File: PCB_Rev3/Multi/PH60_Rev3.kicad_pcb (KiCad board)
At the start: 2 copper layers, 285 x 94.6 mm, 164 parts, among them J1 USB_C_Receptacle_USB2.0_16P

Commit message: muliti layout
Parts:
- removed the S41-x1 at (292.9, 76.2)
- added AE1: Antenna, Library:nrf52_ant_1.6mm, B.Cu at (35.5, 67.4)
- added BT1: Battery, Connector_Molex:Molex_PicoBlade_53261-0271_1x02-1MP_P1.25mm_Horizontal, B.Cu at (231.1, 56.0)
- added C1: 100n, Capacitor_SMD:C_0402_1005Metric, B.Cu at (49.4, 61.9)
- added C10: 12p, Capacitor_SMD:C_0402_1005Metric, B.Cu at (54.2, 60.0)
- added C11: 20u, Capacitor_SMD:C_0402_1005Metric, B.Cu at (12.6, 22.8)
- added C12: 0.5p, Capacitor_SMD:C_0402_1005Metric, B.Cu at (38.5, 65.7)
- added C13: 0.8p, Capacitor_SMD:C_0402_1005Metric, B.Cu at (41.8, 67.0)
- added C14: 12p, Capacitor_SMD:C_0402_1005Metric, B.Cu at (51.1, 74.0)
- added C15: 12p, Capacitor_SMD:C_0402_1005Metric, B.Cu at (49.0, 72.1)
- added C16: 1u, Capacitor_SMD:C_0402_1005Metric, B.Cu at (110.6, 143.8)
- added C17: 47n, Capacitor_SMD:C_0603_1608Metric, B.Cu at (94.2, 138.1)
- added C18: 4u7, Capacitor_SMD:C_0402_1005Metric, B.Cu at (110.6, 145.7)
- added C19: 1u, Capacitor_SMD:C_0402_1005Metric, B.Cu at (110.6, 147.7)
- added C2: 820p, Capacitor_SMD:C_0402_1005Metric, B.Cu at (54.3, 71.7)
- added C20: 100n, Capacitor_SMD:C_0402_1005Metric, B.Cu at (107.7, 137.9)
- added C21: 100n, Capacitor_SMD:C_0402_1005Metric, B.Cu at (107.7, 139.8)
- added C22: 100n, Capacitor_SMD:C_0402_1005Metric, B.Cu at (107.7, 141.8)
- added C3: 4u7, Capacitor_SMD:C_0402_1005Metric, B.Cu at (60.6, 60.4)
- added C4: 100p, Capacitor_SMD:C_0402_1005Metric, B.Cu at (53.2, 71.7)
- added C5: 4u7, Capacitor_SMD:C_0402_1005Metric, B.Cu at (60.4, 64.3)
- added C6: 4u7, Capacitor_SMD:C_0402_1005Metric, B.Cu at (60.6, 59.4)
- added C7: 4u7, Capacitor_SMD:C_0402_1005Metric, B.Cu at (56.6, 60.4)
- added C8: 12p, Capacitor_SMD:C_0402_1005Metric, B.Cu at (48.9, 59.9)
- added C9: 10u, Capacitor_SMD:C_0402_1005Metric, B.Cu at (12.6, 20.9)
- added D14-1: DIODE, Diode_SMD:D_SOD-123, B.Cu at (277.2, 46.4)
- added D61: DIODE, Diode_SMD:D_SOD-123, B.Cu at (120.8, 106.7)
- added D63: DIODE, Diode_SMD:D_SOD-123, B.Cu at (180.7, 107.5)
- added D68: PTVS5V0P1UP, PCM_Diode_SMD_AKL:D_SOD-882_DFN1006-2, B.Cu at (9.80, 21.2)
- added J1: Conn_01x02_Pin, Connector_PinHeader_2.00mm:PinHeader_1x02_P2.00mm_Vertical, B.Cu at (30.4, 81.0)
- added J2: Conn_01x02_Pin, Connector_PinHeader_2.00mm:PinHeader_1x02_P2.00mm_Vertical, B.Cu at (30.4, 73.7)
- added J4: Conn_01x04_Socket, Connector_FFC-FPC:Molex_200528-0040_1x04-1MP_P1.00mm_Horizontal, B.Cu at (97.0, 23.4)
- added L1: MCL1608S100MT, Inductor_SMD:L_0603_1608Metric, B.Cu at (57.9, 59.8)
- added L2: 2.2uH, Inductor_SMD:L_Changjiang_FNR252012S, B.Cu at (15.0, 18.1)
- added L3: FHW0402UC4N7JST, Inductor_SMD:L_0402_1005Metric, B.Cu at (40.1, 67.4)
- added L4: LQG15HS15NJ02D, Inductor_SMD:L_0402_1005Metric, B.Cu at (93.4, 149.9)
- added L5: MCL1608S100MT, Inductor_SMD:L_0603_1608Metric, B.Cu at (94.2, 143.1)
- added R10: 10k, PCM_Resistor_SMD_AKL:R_0402_1005Metric, B.Cu at (24.9, 41.4)
- added R12: 10k, PCM_Resistor_SMD_AKL:R_0402_1005Metric, B.Cu at (15.5, 20.9)
- added R13: 10k, PCM_Resistor_SMD_AKL:R_0402_1005Metric, B.Cu at (15.5, 23.1)
- added R14: 10k, PCM_Resistor_SMD_AKL:R_0402_1005Metric, B.Cu at (21.5, 17.6)
- added R15: 10k, PCM_Resistor_SMD_AKL:R_0402_1005Metric, B.Cu at (21.5, 19.7)
- added R4: 0R, PCM_Resistor_SMD_AKL:R_0603_1608Metric, B.Cu at (37.5, 67.4)
- added R5: 1R, Capacitor_SMD:C_0402_1005Metric, B.Cu at (60.4, 62.2)
- added R6: 1R, Capacitor_SMD:C_0402_1005Metric, B.Cu at (60.4, 63.2)
- added SW1: SW_SPDT_321, Button_Switch_SMD:SW_SPDT_PCM12, B.Cu at (31.4, 49.7)
- added TH1: 10k_NTC, PCM_4ms_Resistor:R_0603, B.Cu at (10.9, 17.5)
- added U2: nRF52840, Library:Nordic_AQFN-73-1EP_7x7mm_P0.5mm_2_Layer_Board, B.Cu at (54.9, 65.9)
- added U4: LGS5500EP, Package_SO:SOIC-8-1EP_3.9x4.9mm_P1.27mm_EP2.41x3.3mm, B.Cu at (56.4, 48.6)
- added X1: 32.768kHz, PCM_Crystal_AKL:Crystal_SMD_3215-2Pin_3.2x1.5mm, B.Cu at (51.5, 59.9)
- added X2: Crystal_Generic, PCM_Crystal_AKL:Crystal_SMD_2016-4Pin_2.0x1.6mm, B.Cu at (51.2, 72.1)
- moved D43 23.7 mm to (271.0, 76.9)
- moved D17 8.55 mm to (70.0, 62.0), turned to 0 degrees
- moved D30 8.02 mm to (49.2, 84.7), turned to 180 degrees
- moved D10 1.00 mm to (185.4, 42.3)
- moved D11 1.00 mm to (204.5, 42.3)
- moved D12 1.00 mm to (223.5, 42.3)
- moved D13 1.00 mm to (242.6, 42.3)
- moved D14 1.00 mm to (261.6, 42.3)
- moved D18 1.00 mm to (80.6, 61.4)
- moved D19 1.00 mm to (99.7, 61.4)
- moved D20 1.00 mm to (118.7, 61.4)
- moved D21 1.00 mm to (137.8, 61.4)
- moved D22 1.00 mm to (156.8, 61.4)
- moved D23 1.00 mm to (175.9, 61.4)
- moved D24 1.00 mm to (194.9, 61.4)
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- renumbered D65 to D1, D9 to D10, D10 to D11, D11 to D12, D12 to D13, D13 to D14, D14 to D15, D15 to D16, D16 to D17, D17 to D18, D18 to D19, D1 to D2, D19 to D20, D20 to D21, D21 to D22, D22 to D23, D23 to D24, D24 to D25, D25 to D26, D26 to D27, D27 to D28, D28 to D29, D2 to D3, D29 to D30, D30 to D31, D31 to D32, D32 to D33, D33 to D34, D34 to D35, D35 to D36, D36 to D37, D37 to D38, D38 to D39, D3 to D4, D39 to D40, D40 to D41, D41 to D42, D42 to D43, D43 to D44, D44 to D45, D45 to D46, D46 to D47, D47 to D48, D48 to D49, D4 to D5, D49 to D50, D50 to D51, D51 to D52, D52 to D53, D53 to D54, D54 to D55, D55 to D56, D56 to D57, D57 to D58, D58 to D59, D5 to D6, D59 to D60, D60 to D62, D61 to D64, D62 to D65, D63 to D66, D64 to D67, D6 to D7, D7 to D8, D8 to D9, J1 to J3, R6 to R7, R7 to R8, S14-2 to S14-1, S14-3 to S14-2, S42 to S29, S29-2 to S29-1, S29 to S30, S30 to S31, S31 to S32, S32 to S33, S33 to S34, S34 to S35, S35 to S36, S36 to S37, S37 to S38, S38 to S39, S39 to S40, S40 to S41, S41-2 to S41-1, S41-x2 to S41-x1, S41 to S42, S43-2 to S43-1, S55-2 to S55-1, S60 to S57, S57-2 to S57-1, S65 to S58, S58-2 to S58-1, S57 to S59, S59-2 to S59-1, S59 to S60, S60-2 to S60-1, S60-x3 to S60-x2, S60-x2 to S60-x3, S61-2 to S61-1, S62-2 to S62-1, S63-2 to S63-1, S64-2 to S64-1, S58 to S65
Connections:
- net VBUS renamed VBUS_USB
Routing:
- net col_13: track 0.00 -> 125.8 mm
- net col_6: track 0.00 -> 119.2 mm
- net col_12: track 0.00 -> 116.7 mm
- net col_0: track 0.00 -> 108.9 mm
- net col_10: track 0.00 -> 103.0 mm
- net col_11: track 0.00 -> 102.7 mm
- net col_1: track 0.00 -> 95.3 mm
- net col_4: track 0.00 -> 90.0 mm
- net col_8: track 0.00 -> 87.0 mm
- net col_7: track 0.00 -> 70.5 mm
- net col_5: track 0.00 -> 67.5 mm
- net col_2: track 0.00 -> 67.5 mm
- net col_9: track 0.00 -> 67.0 mm
- net col_3: track 0.00 -> 44.0 mm
- net Net-(D42-A): track 0.00 -> 41.9 mm
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
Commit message: layout
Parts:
- removed D68: PTVS5V0P1UP, PCM_Diode_SMD_AKL:D_SOD-882_DFN1006-2
- removed SW1: SW_SPDT_321, Button_Switch_SMD:SW_SPDT_PCM12
- moved C16 99.4 mm to (49.3, 65.4)
- moved C18 98.0 mm to (49.9, 68.9), turned to -90 degrees
- moved L4 96.2 mm to (49.3, 64.4)
- moved C21 96.2 mm to (49.3, 63.4)
- moved C19 93.6 mm to (60.4, 68.7), turned to 0 degrees
- moved C20 93.4 mm to (55.6, 60.4), turned to 90 degrees
- moved C22 89.2 mm to (60.3, 66.2), turned to 0 degrees
- moved L5 81.0 mm to (54.5, 72.5), turned to 90 degrees
- moved C17 75.9 mm to (56.0, 72.5), turned to -90 degrees
- moved L2 46.7 mm to (54.6, 42.9)
- moved TH1 46.5 mm to (46.6, 47.2), turned to -90 degrees
- moved R15 45.9 mm to (52.7, 53.3), turned to 90 degrees
- moved C11 44.6 mm to (53.6, 40.4), turned to 90 degrees
- moved C9 44.5 mm to (51.5, 42.6)
- moved R12 41.4 mm to (51.4, 41.6)
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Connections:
- net VBUS renamed /VBUS
- C9 pad 1: VBUS_in -> VBUS_USB
- R10 pad 1: VBUS_in -> VBUS_USB
- R12 pad 1: VBUS_in -> VBUS_USB
- U4 pad 2: VBUS_in -> VBUS_USB
- U4 pad 5: Net-(SW1-B) -> unconnected-(U4-VH-Pad5)
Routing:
- net row_1: track 0.00 -> 263.9 mm, vias 0 -> 2
- net row_0: track 3.47 -> 261.6 mm, vias 0 -> 3
- net row_3: track 0.00 -> 252.0 mm, vias 0 -> 1
- net col_0: track 108.9 -> 357.2 mm
- net row_2: track 2.50 -> 240.1 mm, vias 0 -> 1
- net col_13: track 125.8 -> 163.6 mm, vias 0 -> 1
- net VBUS_USB: track 0.00 -> 22.9 mm, vias 0 -> 4
- net Net-(D44-A): track 15.4 -> 36.0 mm
- net Net-(L4-Pad2): track 0.00 -> 20.2 mm, vias 0 -> 2
- net Net-(D60-A): track 0.00 -> 17.2 mm
- net Net-(D59-A): track 13.0 -> 30.2 mm
- net /DEC4: track 0.00 -> 15.8 mm, vias 0 -> 2
- net col_3: track 44.0 -> 59.5 mm
- net Net-(D45-A): track 0.00 -> 15.5 mm
- net col_2: track 67.5 -> 82.0 mm
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
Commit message: With the basic layout and wiring completed, a simple DRC (Digital Router Control) process is performed.
There is an issue with the satellite axis position that needs to be addressed, and there is also an issue with some pad overlap that needs to be resolved.
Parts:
- added S41-x2: MX_stab, PCM_Mounting_Keyboard_Stabilizer:Stabilizer_Cherry_MX_2.00u, F.Cu at (-0.34, 45.9)
- moved D30 6.87 mm to (55.1, 81.1), turned to 90 degrees
- moved C10 3.47 mm to (51.2, 58.2), turned to 0 degrees
- moved C5 2.34 mm to (62.7, 63.7), turned to -90 degrees
- moved D17 2.11 mm to (57.4, 50.5), turned to -90 degrees
- moved J2 2.09 mm to (30.4, 75.8), turned to 0 degrees
- moved C7 1.45 mm to (56.8, 58.9)
- moved C16 1.42 mm to (47.9, 65.4)
- moved C21 1.42 mm to (47.9, 63.3)
- moved C1 1.42 mm to (48.0, 61.8)
- moved L4 1.42 mm to (47.9, 64.4)
- moved C8 1.01 mm to (49.0, 58.9)
- moved C20 0.95 mm to (55.8, 59.5)
- moved C18 0.62 mm to (49.4, 68.4), turned to 180 degrees
- moved R10 0.40 mm to (50.0, 37.9)
- moved C22 0.16 mm to (60.4, 66.3)
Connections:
- C3 pad 2: /VBUS -> VBUS
- C6 pad 2: /VBUS -> VBUS
- D58 pad 1: col_0 -> row_4
- D59 pad 1: col_0 -> row_4
- D60 pad 1: col_0 -> row_4
- D61 pad 1: col_0 -> row_4
- D62 pad 1: col_0 -> row_4
- D63 pad 1: col_0 -> row_4
- D64 pad 1: col_0 -> row_4
- D65 pad 1: col_0 -> row_4
- D66 pad 1: col_0 -> row_4
- D67 pad 1: col_0 -> row_4
- U2 pad A10: col_1 -> row_0
- U2 pad A12: col_0 -> row_2
- U2 pad A16: unconnected-(U2-P1.13-PadA16) -> row_3
- U2 pad A20: unconnected-(U2-P1.10-PadA20) -> row_4
- U2 pad A8: col_2 -> row_1
- U2 pad AC15: col_6 -> unconnected-(U2-P0.19-PadAC15)
- U2 pad AC17: col_8 -> unconnected-(U2-P0.21-PadAC17)
- U2 pad AC19: col_10 -> unconnected-(U2-P0.23-PadAC19)
- U2 pad AC21: col_12 -> col_1
- U2 pad AC9: col_0 -> unconnected-(U2-P0.14-PadAC9)
- U2 pad AD10: col_4 -> col_7
- U2 pad AD12: col_5 -> col_8
- U2 pad AD16: col_7 -> col_9
- U2 pad AD18: col_9 -> col_10
- U2 pad AD2: /VBUS -> VBUS
- U2 pad AD22: col_13 -> col_12
- U2 pad AD8: col_3 -> col_6
- U2 pad G1: /LED_VDD -> col_14
- U2 pad J1: unconnected-(U2-AIN2/P0.04-PadJ1) -> col_5
- U2 pad L1: row_3 -> col_4
- U2 pad N1: row_2 -> col_3
- U2 pad R1: row_1 -> col_2
- U2 pad U1: row_0 -> unconnected-(U2-TRACEDATA1/P0.12-PadU1)
- U2 pad Y2: /VBUS -> VBUS
- U2 pad Y23: unconnected-(U2-P1.01-PadY23) -> col_0
- U4 pad 5: unconnected-(U4-VH-Pad5) -> VBUS
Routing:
- net row_4: track 0.00 -> 288.8 mm, vias 0 -> 2
- net col_14: track 0.00 -> 259.6 mm, vias 0 -> 3
- net col_12: track 110.5 -> 338.9 mm, vias 0 -> 2
- net col_0: track 357.2 -> 158.1 mm, vias 0 -> 2
- net col_11: track 95.2 -> 291.0 mm
- net +BATT: track 5.05 -> 192.4 mm, vias 0 -> 7
- net col_10: track 95.5 -> 271.4 mm
- net col_9: track 59.7 -> 219.9 mm
- net col_8: track 79.5 -> 219.4 mm
- net col_7: track 60.0 -> 180.0 mm
- net col_6: track 111.7 -> 207.0 mm
- net col_5: track 60.0 -> 153.2 mm, vias 0 -> 3
- net col_4: track 82.8 -> 153.4 mm, vias 0 -> 3
- net row_3: track 252.0 -> 315.8 mm, vias 1 -> 4
- net /USB_D-: track 7.23 -> 62.8 mm, vias 0 -> 3
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
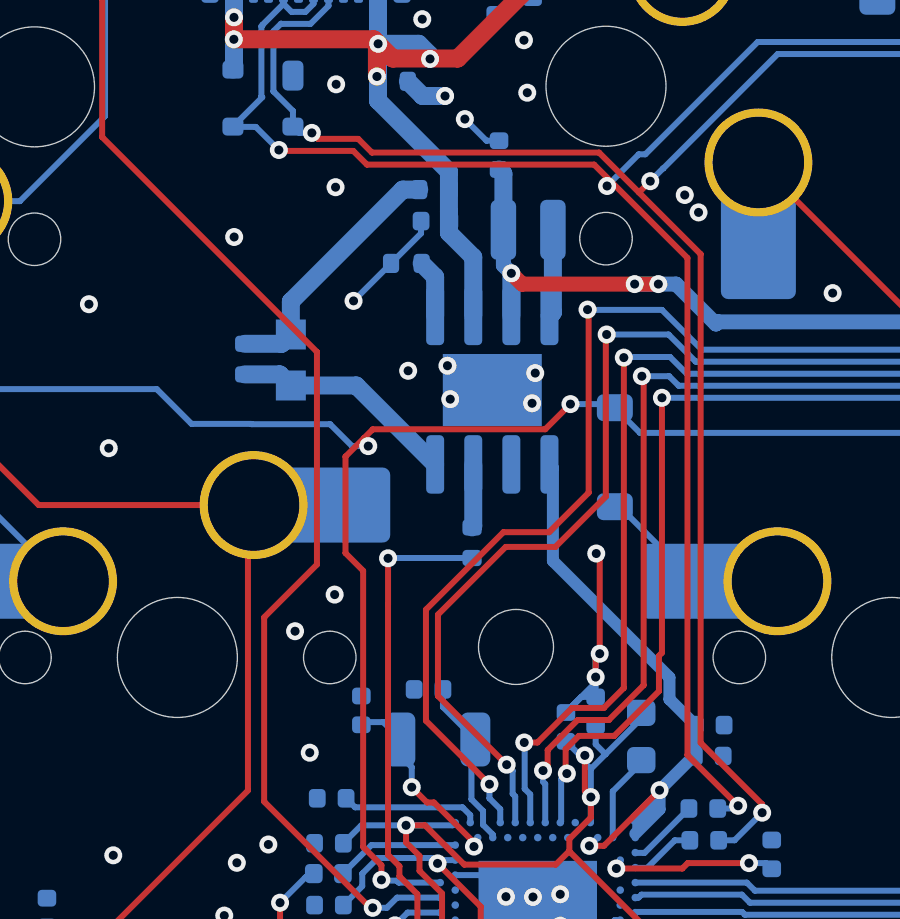
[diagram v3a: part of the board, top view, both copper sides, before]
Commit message: Delete RGB
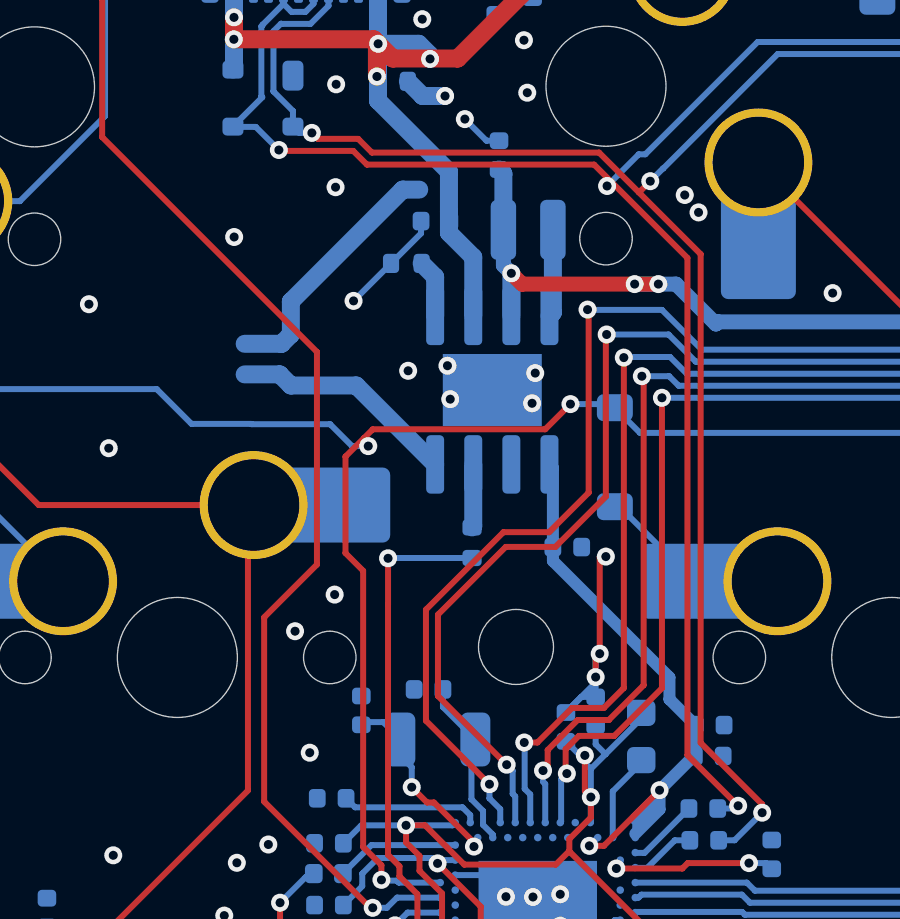
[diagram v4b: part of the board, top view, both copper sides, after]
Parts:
- removed R12, R13: 10k, PCM_Resistor_SMD_AKL:R_0402_1005Metric
- removed TH1: 10k_NTC, PCM_4ms_Resistor:R_0603
- added C24: 20u, Capacitor_SMD:C_0402_1005Metric, B.Cu at (55.9, 53.5)
- R10: value 10k -> 1k
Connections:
- R10 pad 1: VBUS_USB -> GND
- R10 pad 2: GND -> VBUS_USB
- R14 pad 1: GND -> Net-(U4-ISET)
- R14 pad 2: Net-(U4-ISET) -> GND
- S59-1 pad 1: unconnected-(S59-1-Pad1) -> col_2
- S59-1 pad 2: unconnected-(S59-1-Pad2) -> Net-(D60-A)
- U4 pad 8: Net-(U4-NTC) -> GND
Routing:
- net Net-(R12-Pad2): track 8.59 -> 0.00 mm
- net (no net): track 0.00 -> 8.59 mm
- net Net-(U4-NTC): track 7.59 -> 0.00 mm
- net GND: track 20.9 -> 27.1 mm
- net VBUS_USB: track 53.2 -> 54.6 mm
